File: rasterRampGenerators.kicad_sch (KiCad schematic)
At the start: 40 parts, among them J2 H_Sync, J3 V_Sync, Q1 2N7000, Q10 2N7000, Q11 2N7000, Q12 2N7000, Q13 2N7000, Q14 2N7000, Q15 2N7000, Q2 2N7000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

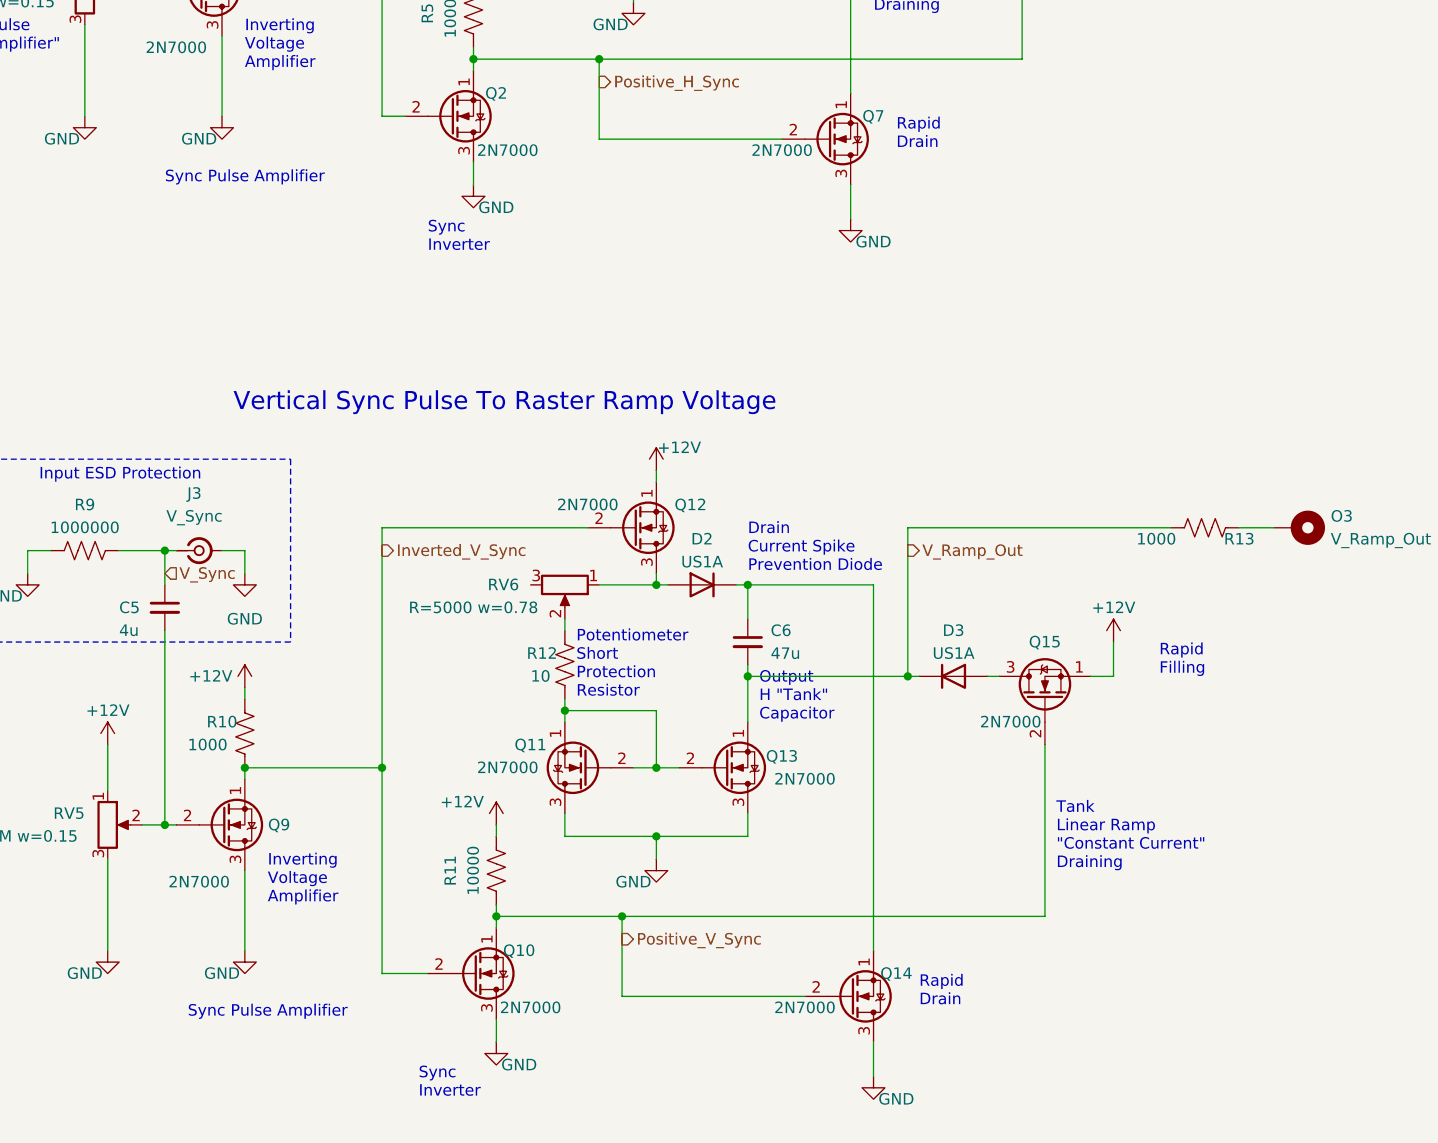
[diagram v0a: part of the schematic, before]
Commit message: linked models so spice simulation runs
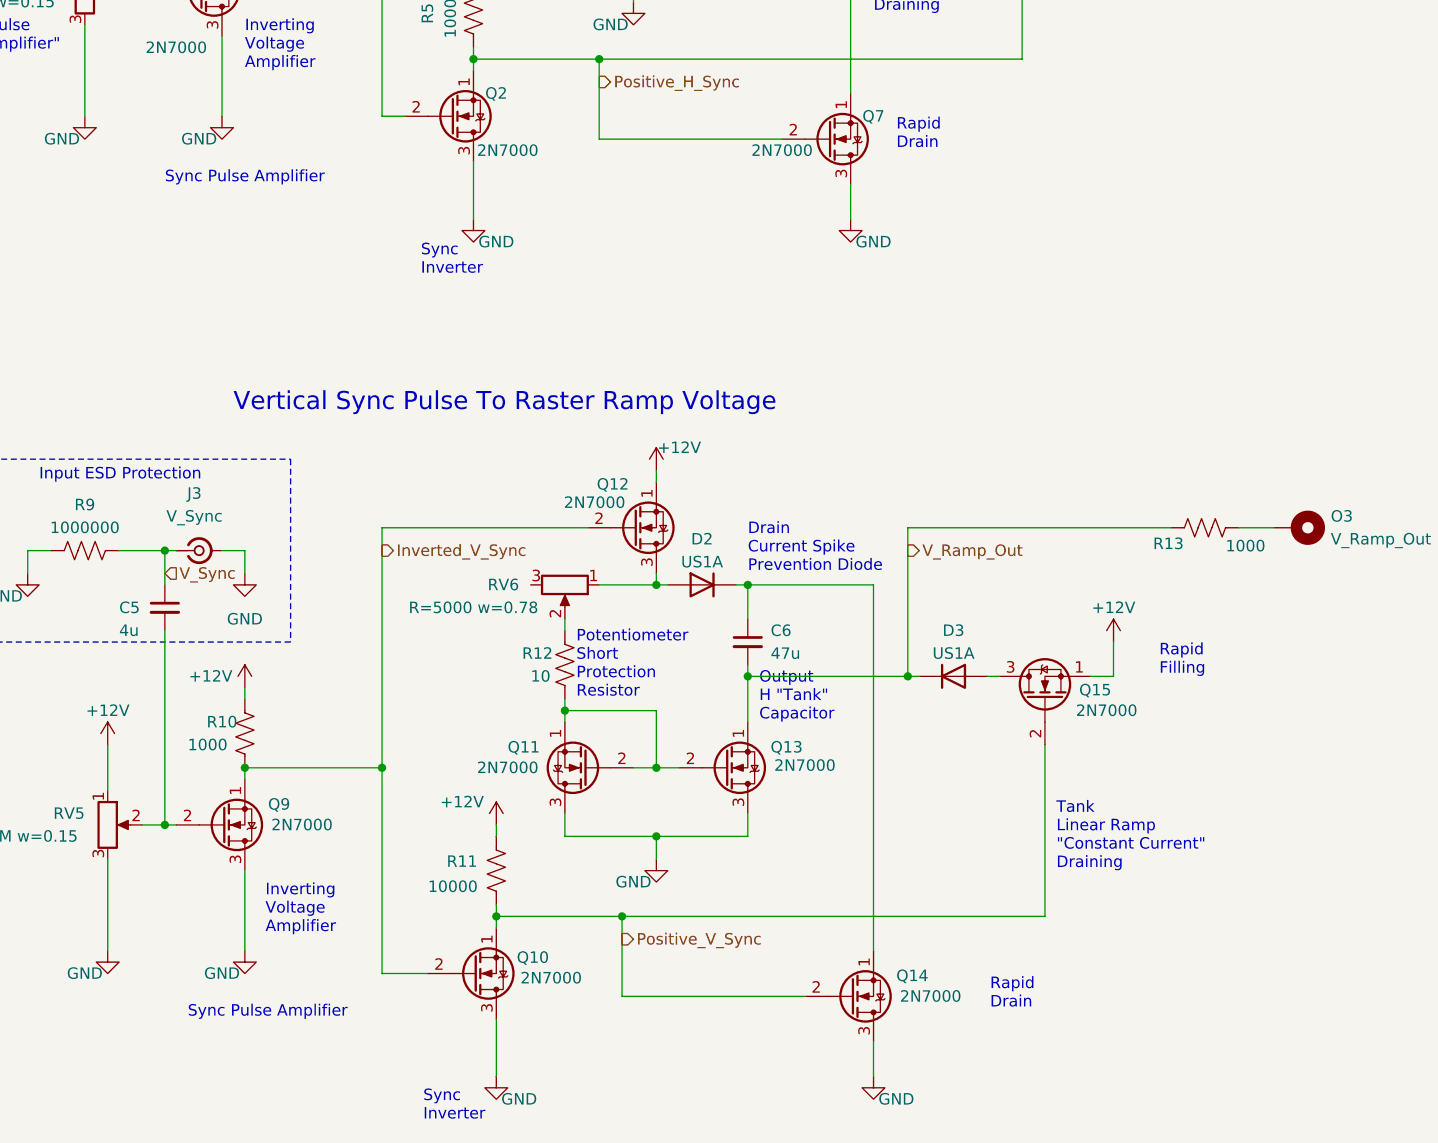
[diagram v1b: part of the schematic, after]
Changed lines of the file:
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@@
 	(wire
 		(pts
-			(xy 80.01 86.36) (xy 80.01 88.9)
+			(xy 80.01 86.36) (xy 80.01 92.71)
 		)
 		(stroke
@@
 	(wire
 		(pts
-			(xy 82.55 181.61) (xy 82.55 184.15)
+			(xy 82.55 181.61) (xy 82.55 187.96)
 		)
 		(stroke
@@
 	(text "Sync\nInverter"
 		(exclude_from_sim no)
-		(at 74.93 96.52 0)
+		(at 74.168 99.06 0)
 		(effects
 			(font
@@
 	(text "Sync\nInverter"
 		(exclude_from_sim no)
-		(at 73.914 190.5 0)
+		(at 74.422 193.04 0)
 		(effects
 			(font
@@
 	(text "Rapid\nDrain"
 		(exclude_from_sim no)
-		(at 129.54 180.34 0)
+		(at 137.414 180.594 0)
 		(effects
 			(font
@@
 	(text "Inverting\nVoltage\nAmplifier"
 		(exclude_from_sim no)
-		(at 57.15 168.91 0)
+		(at 56.896 172.212 0)
 		(effects
 			(font
@@
 	(symbol
 		(lib_id "power:GND")
-		(at 82.55 184.15 0)
+		(at 82.55 187.96 0)
 		(unit 1)
 		(exclude_from_sim no)
@@
 		(dnp no)
 		(property "Reference" "#PWR032"
-			(at 82.55 190.5 0)
+			(at 82.55 194.31 0)
 			(effects
 				(font
@@
 		)
 		(property "Value" "GND"
-			(at 85.09 186.69 0)
+			(at 85.09 190.5 0)
 			(effects
 				(font
@@
 		)
 		(property "Footprint" ""
-			(at 82.55 184.15 0)
+			(at 82.55 187.96 0)
 			(effects
 				(font
@@
 		)
 		(property "Datasheet" ""
-			(at 82.55 184.15 0)
+			(at 82.55 187.96 0)
 			(effects
 				(font
@@
 		)
 		(property "Description" ""
-			(at 82.55 184.15 0)
+			(at 82.55 187.96 0)
 			(effects
 				(font
@@
 		)
 		(property "Sim.Device" "V"
-			(at 82.55 184.15 0)
+			(at 82.55 187.96 0)
 			(effects
 				(font
@@
 		)
 		(property "Sim.Type" "DC"
-			(at 82.55 184.15 0)
+			(at 82.55 187.96 0)
 			(effects
 				(font
@@
 		)
 		(property "Sim.Pins" "1=+"
-			(at 82.55 184.15 0)
+			(at 82.55 187.96 0)
 			(effects
 				(font
@@
 		)
 		(property "Sim.Params" "dc=0"
-			(at 82.55 184.15 0)
+			(at 82.55 187.96 0)
 			(effects
 				(font
@@
 		(dnp no)
 		(property "Reference" "Q13"
-			(at 114.3 152.4 0)
+			(at 114.808 151.384 0)
 			(effects
 				(font
@@
 		)
 		(property "Value" "2N7000"
-			(at 116.84 154.94 0)
+			(at 116.84 153.416 0)
 			(effects
 				(font
@@
 		(dnp no)
 		(property "Reference" "Q10"
-			(at 85.09 173.99 0)
+			(at 86.614 174.752 0)
 			(effects
 				(font
@@
 		)
 		(property "Value" "2N7000"
-			(at 86.36 180.34 0)
+			(at 88.646 177.038 0)
 			(effects
 				(font
@@
 		(dnp no)
 		(property "Reference" "Q12"
-			(at 104.14 124.46 0)
+			(at 95.504 122.174 0)
 			(effects
 				(font
@@
 		)
 		(property "Value" "2N7000"
-			(at 92.71 124.46 0)
+			(at 93.472 124.206 0)
 			(effects
 				(font
@@
 		(dnp no)
 		(property "Reference" "R11"
-			(at 77.47 165.1 90)
+			(at 78.74 164.084 0)
 			(effects
 				(font
@@
 		)
 		(property "Value" "10000"
-			(at 80.01 165.1 90)
+			(at 77.724 166.878 0)
 			(effects
 				(font
@@
 		(dnp no)
 		(property "Reference" "R13"
-			(at 165.1 128.27 90)
+			(at 157.226 128.778 90)
 			(effects
 				(font
@@
 		)
 		(property "Value" "1000"
-			(at 153.67 128.27 90)
+			(at 163.576 129.032 90)
 			(effects
 				(font
@@
 		(dnp no)
 		(property "Reference" "Q11"
-			(at 86.36 151.13 0)
+			(at 85.598 151.384 0)
 			(effects
 				(font
@@
 		(dnp no)
 		(property "Reference" "Q14"
-			(at 127 176.53 0)
+			(at 128.778 176.784 0)
 			(effects
 				(font
@@
 		)
 		(property "Value" "2N7000"
-			(at 116.84 180.34 0)
+			(at 130.81 179.07 0)
 			(effects
 				(font
@@
 		(dnp no)
 		(property "Reference" "Q15"
-			(at 143.51 139.7 90)
+			(at 149.098 145.034 90)
 			(effects
 				(font
@@
 		)
 		(property "Value" "2N7000"
-			(at 139.7 148.59 90)
+			(at 150.368 147.32 90)
 			(effects
 				(font
@@
 		(dnp no)
 		(property "Reference" "R12"
-			(at 87.63 140.97 0)
+			(at 87.122 140.97 0)
 			(effects
 				(font
@@
 	(symbol
 		(lib_id "power:GND")
-		(at 80.01 88.9 0)
+		(at 80.01 92.71 0)
 		(unit 1)
 		(exclude_from_sim no)
@@
 		(dnp no)
 		(property "Reference" "#PWR011"
-			(at 80.01 95.25 0)
+			(at 80.01 99.06 0)
 			(effects
 				(font
@@
 		)
 		(property "Value" "GND"
-			(at 82.55 91.44 0)
+			(at 82.55 95.25 0)
 			(effects
 				(font
@@
 		)
 		(property "Footprint" ""
-			(at 80.01 88.9 0)
+			(at 80.01 92.71 0)
 			(effects
 				(font
@@
 		)
 		(property "Datasheet" ""
-			(at 80.01 88.9 0)
+			(at 80.01 92.71 0)
 			(effects
 				(font
@@
 		)
 		(property "Description" ""
-			(at 80.01 88.9 0)
+			(at 80.01 92.71 0)
 			(effects
 				(font
@@
 		)
 		(property "Sim.Device" "V"
-			(at 80.01 88.9 0)
+			(at 80.01 92.71 0)
 			(effects
 				(font
@@
 		)
 		(property "Sim.Type" "DC"
-			(at 80.01 88.9 0)
+			(at 80.01 92.71 0)
 			(effects
 				(font
@@
 		)
 		(property "Sim.Pins" "1=+"
-			(at 80.01 88.9 0)
+			(at 80.01 92.71 0)
 			(effects
 				(font
@@
 		)
 		(property "Sim.Params" "dc=0"
-			(at 80.01 88.9 0)
+			(at 80.01 92.71 0)
 			(effects
 				(font
@@
 		(dnp no)
 		(property "Reference" "Q9"
-			(at 58.42 160.02 0)
+			(at 58.42 157.734 0)
 			(effects
 				(font
@@
 		)
 		(property "Value" "2N7000"
-			(at 49.53 166.37 0)
+			(at 60.96 160.02 0)
 			(effects
 				(font

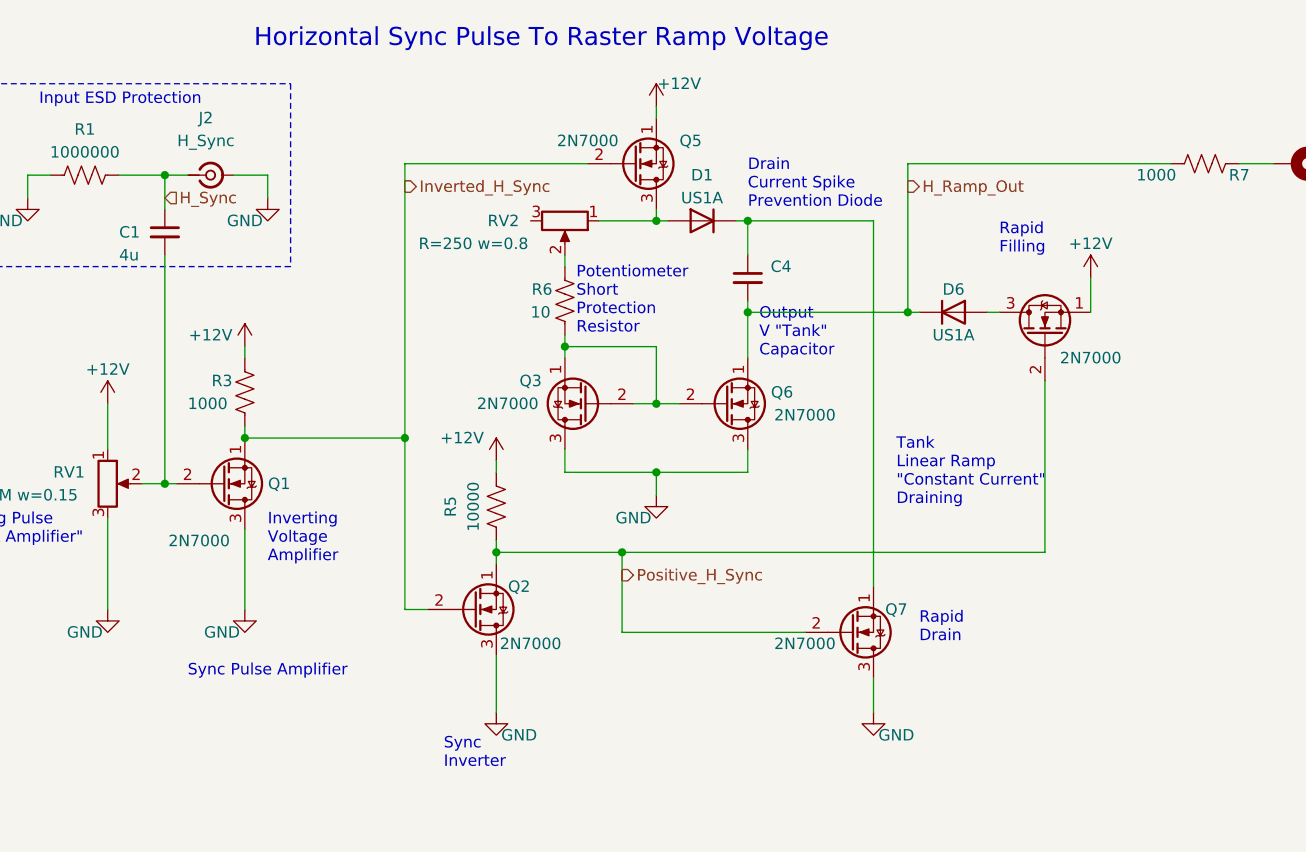
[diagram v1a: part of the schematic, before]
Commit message: added new spice directives to improve simulation speed, added sections for motor drivers, micro controlers, i2c bus connections, realized that focusing coils, hv, horizontal and vertical ramp will need time stable signals (not voltage dependant like with a voltage controlled oscilator) so it will be much simpler to design them with micro controllers
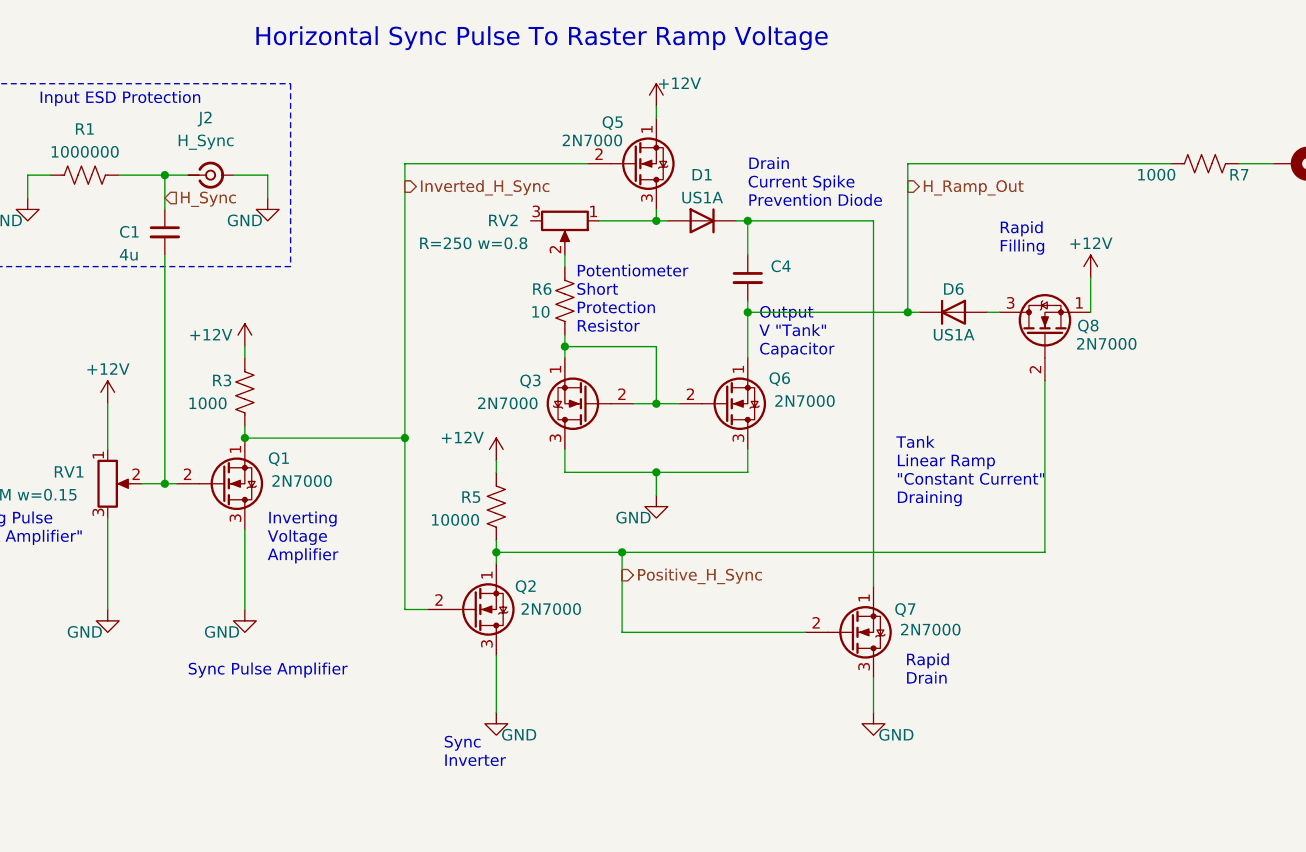
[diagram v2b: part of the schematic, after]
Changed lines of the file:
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@@
 	(text "Rapid\nDrain"
 		(exclude_from_sim no)
-		(at 127 85.09 0)
+		(at 125.476 89.916 0)
 		(effects
 			(font
@@
 		(dnp no)
 		(property "Reference" "Q1"
-			(at 55.88 67.31 0)
+			(at 55.88 64.516 0)
 			(effects
 				(font
@@
 		)
 		(property "Value" "2N7000"
-			(at 46.99 73.66 0)
+			(at 58.42 67.056 0)
 			(effects
 				(font
@@
 		(dnp no)
 		(property "Reference" "R5"
-			(at 74.93 69.85 90)
+			(at 77.216 68.834 0)
 			(effects
 				(font
@@
 		)
 		(property "Value" "10000"
-			(at 77.47 69.85 90)
+			(at 75.438 71.374 0)
 			(effects
 				(font
@@
 		(dnp no)
 		(property "Reference" "Q8"
-			(at 140.97 44.45 90)
+			(at 145.796 49.784 90)
 			(effects
 				(font
 					(size 1.27 1.27)
 				)
-				(hide yes)
 			)
 		)
 		(property "Value" "2N7000"
-			(at 146.05 53.34 90)
+			(at 147.828 51.816 90)
 			(effects
 				(font
@@
 		(dnp no)
 		(property "Reference" "Q7"
-			(at 124.46 81.28 0)
+			(at 125.476 81.28 0)
 			(effects
 				(font
@@
 		)
 		(property "Value" "2N7000"
-			(at 114.3 85.09 0)
+			(at 128.27 83.566 0)
 			(effects
 				(font
@@
 		(dnp no)
 		(property "Reference" "Q5"
-			(at 101.6 29.21 0)
+			(at 92.964 27.178 0)
 			(effects
 				(font
@@
 		)
 		(property "Value" "2N7000"
-			(at 90.17 29.21 0)
+			(at 90.678 29.21 0)
 			(effects
 				(font
@@
 		(dnp no)
 		(property "Reference" "Q2"
-			(at 82.55 78.74 0)
+			(at 83.312 78.74 0)
 			(effects
 				(font
@@
 		)
 		(property "Value" "2N7000"
-			(at 83.82 85.09 0)
+			(at 86.106 81.28 0)
 			(effects
 				(font
@@
 		(dnp no)
 		(property "Reference" "Q6"
-			(at 111.76 57.15 0)
+			(at 111.506 55.626 0)
 			(effects
 				(font
@@
 		)
 		(property "Value" "2N7000"
-			(at 114.3 59.69 0)
+			(at 114.3 58.166 0)
 			(effects
 				(font
